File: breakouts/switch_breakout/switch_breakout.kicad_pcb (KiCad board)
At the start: 4 copper layers, 35.5 x 27.8 mm, 10 parts, among them P1 CONN_01X03, U101 CONN_SMA_2GND, U102 CONN_SMA_2GND, U103 CONN_SMA_2GND, U3 PE42521

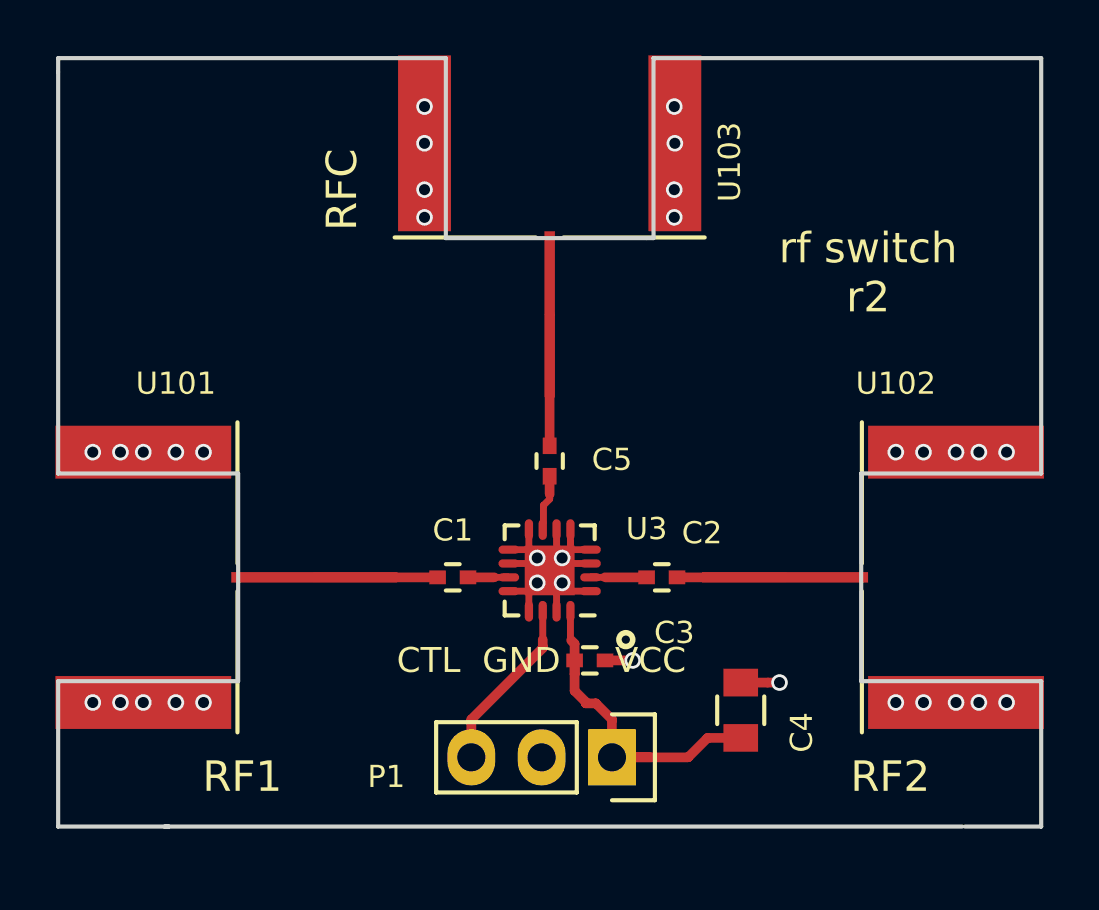
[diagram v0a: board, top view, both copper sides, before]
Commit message: switched switch board to be coplanar waveguide fed
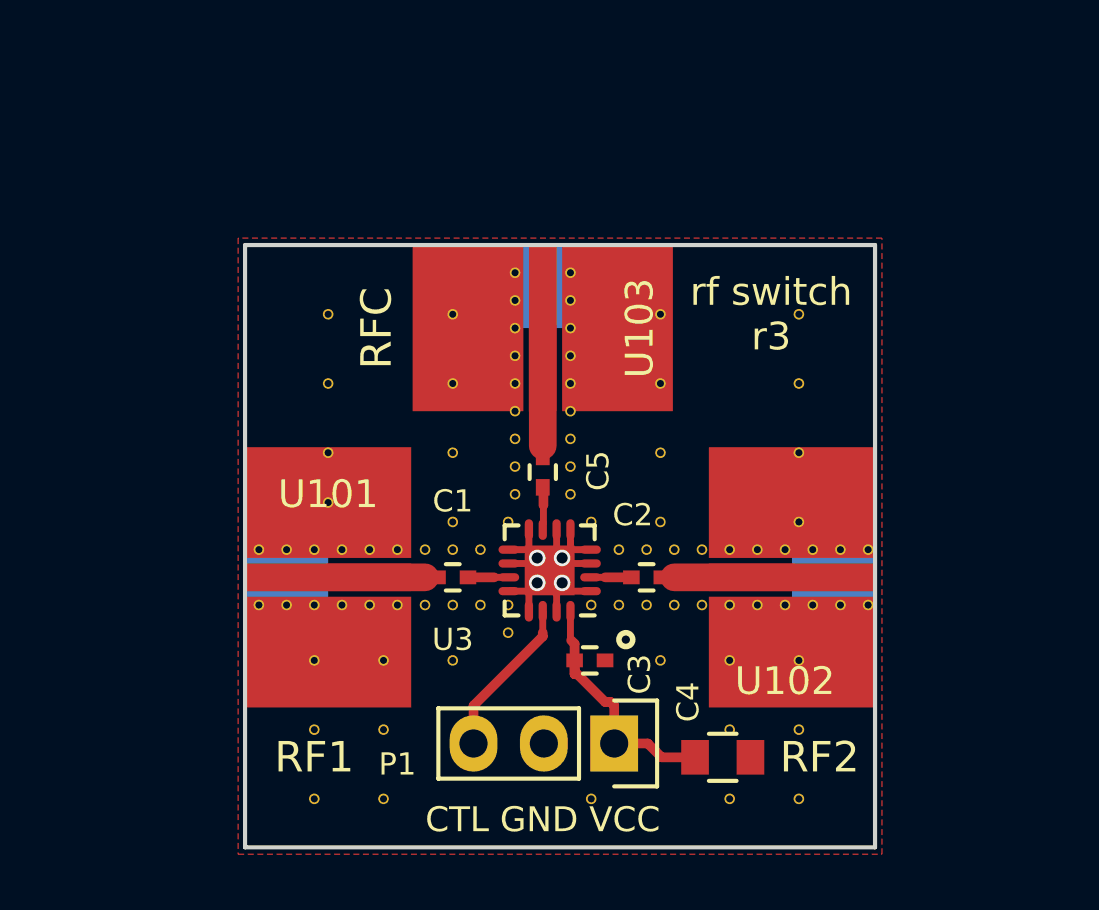
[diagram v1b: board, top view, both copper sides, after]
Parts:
- added REF**: VIA_OSH4LAYER_MIN, vna_footprints:VIA_OSH4LAYER_MIN, F.Cu at (145.0, 110.0)
- added REF**: VIA_OSH4LAYER_MIN, vna_footprints:VIA_OSH4LAYER_MIN, F.Cu at (152.5, 105.0)
- added REF**: VIA_OSH4LAYER_MIN, vna_footprints:VIA_OSH4LAYER_MIN, F.Cu at (145.0, 105.0)
- added REF**: VIA_OSH4LAYER_MIN, vna_footprints:VIA_OSH4LAYER_MIN, F.Cu at (145.0, 102.5)
- added REF**: VIA_OSH4LAYER_MIN, vna_footprints:VIA_OSH4LAYER_MIN, F.Cu at (145.0, 100.0)
- added REF**: VIA_OSH4LAYER_MIN, vna_footprints:VIA_OSH4LAYER_MIN, F.Cu at (145.0, 97.5)
- added REF**: VIA_OSH4LAYER_MIN, vna_footprints:VIA_OSH4LAYER_MIN, F.Cu at (140.5, 97.5)
- added REF**: VIA_OSH4LAYER_MIN, vna_footprints:VIA_OSH4LAYER_MIN, F.Cu at (140.5, 100.0)
- added REF**: VIA_OSH4LAYER_MIN, vna_footprints:VIA_OSH4LAYER_MIN, F.Cu at (140.5, 102.5)
- added REF**: VIA_OSH4LAYER_MIN, vna_footprints:VIA_OSH4LAYER_MIN, F.Cu at (140.5, 104.3)
- added REF**: VIA_OSH4LAYER_MIN, vna_footprints:VIA_OSH4LAYER_MIN, F.Cu at (140.0, 115.0)
- added REF**: VIA_OSH4LAYER_MIN, vna_footprints:VIA_OSH4LAYER_MIN, F.Cu at (150.0, 115.0)
- added REF**: VIA_OSH4LAYER_MIN, vna_footprints:VIA_OSH4LAYER_MIN, F.Cu at (142.5, 115.0)
- added REF**: VIA_OSH4LAYER_MIN, vna_footprints:VIA_OSH4LAYER_MIN, F.Cu at (142.5, 112.5)
- added REF**: VIA_OSH4LAYER_MIN, vna_footprints:VIA_OSH4LAYER_MIN, F.Cu at (140.0, 112.5)
- added REF**: VIA_OSH4LAYER_MIN, vna_footprints:VIA_OSH4LAYER_MIN, F.Cu at (140.0, 110.0)
- added REF**: VIA_OSH4LAYER_MIN, vna_footprints:VIA_OSH4LAYER_MIN, F.Cu at (142.5, 110.0)
- added REF**: VIA_OSH4LAYER_MIN, vna_footprints:VIA_OSH4LAYER_MIN, F.Cu at (157.5, 110.0)
- added REF**: VIA_OSH4LAYER_MIN, vna_footprints:VIA_OSH4LAYER_MIN, F.Cu at (157.5, 112.5)
- added REF**: VIA_OSH4LAYER_MIN, vna_footprints:VIA_OSH4LAYER_MIN, F.Cu at (157.5, 115.0)
- added REF**: VIA_OSH4LAYER_MIN, vna_footprints:VIA_OSH4LAYER_MIN, F.Cu at (155.0, 115.0)
- added REF**: VIA_OSH4LAYER_MIN, vna_footprints:VIA_OSH4LAYER_MIN, F.Cu at (155.0, 112.5)
- added REF**: VIA_OSH4LAYER_MIN, vna_footprints:VIA_OSH4LAYER_MIN, F.Cu at (152.5, 97.5)
- added REF**: VIA_OSH4LAYER_MIN, vna_footprints:VIA_OSH4LAYER_MIN, F.Cu at (155.0, 110.0)
- added REF**: VIA_OSH4LAYER_MIN, vna_footprints:VIA_OSH4LAYER_MIN, F.Cu at (152.5, 110.0)
- added REF**: VIA_OSH4LAYER_MIN, vna_footprints:VIA_OSH4LAYER_MIN, F.Cu at (150.0, 105.0)
- added REF**: VIA_OSH4LAYER_MIN, vna_footprints:VIA_OSH4LAYER_MIN, F.Cu at (149.2, 96.0)
- added REF**: VIA_OSH4LAYER_MIN, vna_footprints:VIA_OSH4LAYER_MIN, F.Cu at (149.2, 97.0)
- added REF**: VIA_OSH4LAYER_MIN, vna_footprints:VIA_OSH4LAYER_MIN, F.Cu at (149.2, 98.0)
- added REF**: VIA_OSH4LAYER_MIN, vna_footprints:VIA_OSH4LAYER_MIN, F.Cu at (149.2, 99.0)
- added REF**: VIA_OSH4LAYER_MIN, vna_footprints:VIA_OSH4LAYER_MIN, F.Cu at (149.2, 100.0)
- added REF**: VIA_OSH4LAYER_MIN, vna_footprints:VIA_OSH4LAYER_MIN, F.Cu at (149.2, 101.0)
- added REF**: VIA_OSH4LAYER_MIN, vna_footprints:VIA_OSH4LAYER_MIN, F.Cu at (149.2, 104.0)
- added REF**: VIA_OSH4LAYER_MIN, vna_footprints:VIA_OSH4LAYER_MIN, F.Cu at (157.5, 97.5)
- added REF**: VIA_OSH4LAYER_MIN, vna_footprints:VIA_OSH4LAYER_MIN, F.Cu at (149.2, 103.0)
- added REF**: VIA_OSH4LAYER_MIN, vna_footprints:VIA_OSH4LAYER_MIN, F.Cu at (149.2, 102.0)
- added REF**: VIA_OSH4LAYER_MIN, vna_footprints:VIA_OSH4LAYER_MIN, F.Cu at (138.0, 108.0)
- added REF**: VIA_OSH4LAYER_MIN, vna_footprints:VIA_OSH4LAYER_MIN, F.Cu at (138.0, 106.0)
- added REF**: VIA_OSH4LAYER_MIN, vna_footprints:VIA_OSH4LAYER_MIN, F.Cu at (139.0, 106.0)
- added REF**: VIA_OSH4LAYER_MIN, vna_footprints:VIA_OSH4LAYER_MIN, F.Cu at (140.0, 106.0)
- added REF**: VIA_OSH4LAYER_MIN, vna_footprints:VIA_OSH4LAYER_MIN, F.Cu at (141.0, 106.0)
- added REF**: VIA_OSH4LAYER_MIN, vna_footprints:VIA_OSH4LAYER_MIN, F.Cu at (142.0, 106.0)
- added REF**: VIA_OSH4LAYER_MIN, vna_footprints:VIA_OSH4LAYER_MIN, F.Cu at (143.0, 106.0)
- added REF**: VIA_OSH4LAYER_MIN, vna_footprints:VIA_OSH4LAYER_MIN, F.Cu at (144.0, 106.0)
- added REF**: VIA_OSH4LAYER_MIN, vna_footprints:VIA_OSH4LAYER_MIN, F.Cu at (157.5, 100.0)
- added REF**: VIA_OSH4LAYER_MIN, vna_footprints:VIA_OSH4LAYER_MIN, F.Cu at (145.0, 106.0)
- added REF**: VIA_OSH4LAYER_MIN, vna_footprints:VIA_OSH4LAYER_MIN, F.Cu at (151.0, 106.0)
- added REF**: VIA_OSH4LAYER_MIN, vna_footprints:VIA_OSH4LAYER_MIN, F.Cu at (152.0, 106.0)
- added REF**: VIA_OSH4LAYER_MIN, vna_footprints:VIA_OSH4LAYER_MIN, F.Cu at (153.0, 106.0)
- added REF**: VIA_OSH4LAYER_MIN, vna_footprints:VIA_OSH4LAYER_MIN, F.Cu at (154.0, 106.0)
- added REF**: VIA_OSH4LAYER_MIN, vna_footprints:VIA_OSH4LAYER_MIN, F.Cu at (155.0, 106.0)
- added REF**: VIA_OSH4LAYER_MIN, vna_footprints:VIA_OSH4LAYER_MIN, F.Cu at (156.0, 106.0)
- added REF**: VIA_OSH4LAYER_MIN, vna_footprints:VIA_OSH4LAYER_MIN, F.Cu at (157.0, 106.0)
- added REF**: VIA_OSH4LAYER_MIN, vna_footprints:VIA_OSH4LAYER_MIN, F.Cu at (158.0, 106.0)
- added REF**: VIA_OSH4LAYER_MIN, vna_footprints:VIA_OSH4LAYER_MIN, F.Cu at (159.0, 106.0)
- added REF**: VIA_OSH4LAYER_MIN, vna_footprints:VIA_OSH4LAYER_MIN, F.Cu at (152.5, 100.0)
- added REF**: VIA_OSH4LAYER_MIN, vna_footprints:VIA_OSH4LAYER_MIN, F.Cu at (160.0, 106.0)
- added REF**: VIA_OSH4LAYER_MIN, vna_footprints:VIA_OSH4LAYER_MIN, F.Cu at (160.0, 108.0)
- added REF**: VIA_OSH4LAYER_MIN, vna_footprints:VIA_OSH4LAYER_MIN, F.Cu at (159.0, 108.0)
- added REF**: VIA_OSH4LAYER_MIN, vna_footprints:VIA_OSH4LAYER_MIN, F.Cu at (158.0, 108.0)
- added REF**: VIA_OSH4LAYER_MIN, vna_footprints:VIA_OSH4LAYER_MIN, F.Cu at (157.0, 108.0)
- added REF**: VIA_OSH4LAYER_MIN, vna_footprints:VIA_OSH4LAYER_MIN, F.Cu at (156.0, 108.0)
- added REF**: VIA_OSH4LAYER_MIN, vna_footprints:VIA_OSH4LAYER_MIN, F.Cu at (155.0, 108.0)
- added REF**: VIA_OSH4LAYER_MIN, vna_footprints:VIA_OSH4LAYER_MIN, F.Cu at (154.0, 108.0)
- added REF**: VIA_OSH4LAYER_MIN, vna_footprints:VIA_OSH4LAYER_MIN, F.Cu at (153.0, 108.0)
- added REF**: VIA_OSH4LAYER_MIN, vna_footprints:VIA_OSH4LAYER_MIN, F.Cu at (152.0, 108.0)
- added REF**: VIA_OSH4LAYER_MIN, vna_footprints:VIA_OSH4LAYER_MIN, F.Cu at (152.5, 102.5)
- added REF**: VIA_OSH4LAYER_MIN, vna_footprints:VIA_OSH4LAYER_MIN, F.Cu at (151.0, 108.0)
- added REF**: VIA_OSH4LAYER_MIN, vna_footprints:VIA_OSH4LAYER_MIN, F.Cu at (150.0, 108.0)
- added REF**: VIA_OSH4LAYER_MIN, vna_footprints:VIA_OSH4LAYER_MIN, F.Cu at (147.2, 96.0)
- added REF**: VIA_OSH4LAYER_MIN, vna_footprints:VIA_OSH4LAYER_MIN, F.Cu at (147.2, 97.0)
- added REF**: VIA_OSH4LAYER_MIN, vna_footprints:VIA_OSH4LAYER_MIN, F.Cu at (147.2, 98.0)
- added REF**: VIA_OSH4LAYER_MIN, vna_footprints:VIA_OSH4LAYER_MIN, F.Cu at (147.2, 99.0)
- added REF**: VIA_OSH4LAYER_MIN, vna_footprints:VIA_OSH4LAYER_MIN, F.Cu at (147.2, 100.0)
- added REF**: VIA_OSH4LAYER_MIN, vna_footprints:VIA_OSH4LAYER_MIN, F.Cu at (147.2, 101.0)
- added REF**: VIA_OSH4LAYER_MIN, vna_footprints:VIA_OSH4LAYER_MIN, F.Cu at (147.2, 102.0)
- added REF**: VIA_OSH4LAYER_MIN, vna_footprints:VIA_OSH4LAYER_MIN, F.Cu at (147.2, 103.0)
- added REF**: VIA_OSH4LAYER_MIN, vna_footprints:VIA_OSH4LAYER_MIN, F.Cu at (157.5, 102.5)
- added REF**: VIA_OSH4LAYER_MIN, vna_footprints:VIA_OSH4LAYER_MIN, F.Cu at (147.2, 104.0)
- added REF**: VIA_OSH4LAYER_MIN, vna_footprints:VIA_OSH4LAYER_MIN, F.Cu at (147.0, 105.0)
- added REF**: VIA_OSH4LAYER_MIN, vna_footprints:VIA_OSH4LAYER_MIN, F.Cu at (146.0, 106.0)
- added REF**: VIA_OSH4LAYER_MIN, vna_footprints:VIA_OSH4LAYER_MIN, F.Cu at (147.0, 109.0)
- added REF**: VIA_OSH4LAYER_MIN, vna_footprints:VIA_OSH4LAYER_MIN, F.Cu at (147.0, 108.0)
- added REF**: VIA_OSH4LAYER_MIN, vna_footprints:VIA_OSH4LAYER_MIN, F.Cu at (146.0, 108.0)
- added REF**: VIA_OSH4LAYER_MIN, vna_footprints:VIA_OSH4LAYER_MIN, F.Cu at (145.0, 108.0)
- added REF**: VIA_OSH4LAYER_MIN, vna_footprints:VIA_OSH4LAYER_MIN, F.Cu at (144.0, 108.0)
- added REF**: VIA_OSH4LAYER_MIN, vna_footprints:VIA_OSH4LAYER_MIN, F.Cu at (143.0, 108.0)
- added REF**: VIA_OSH4LAYER_MIN, vna_footprints:VIA_OSH4LAYER_MIN, F.Cu at (142.0, 108.0)
- added REF**: VIA_OSH4LAYER_MIN, vna_footprints:VIA_OSH4LAYER_MIN, F.Cu at (157.5, 105.0)
- added REF**: VIA_OSH4LAYER_MIN, vna_footprints:VIA_OSH4LAYER_MIN, F.Cu at (141.0, 108.0)
- added REF**: VIA_OSH4LAYER_MIN, vna_footprints:VIA_OSH4LAYER_MIN, F.Cu at (140.0, 108.0)
- added REF**: VIA_OSH4LAYER_MIN, vna_footprints:VIA_OSH4LAYER_MIN, F.Cu at (139.0, 108.0)
- U101, U102, U103: footprint vna_footprints:142-0721-882_sma_cutout -> vna_footprints:SMA_CPW_1MM_.2MM
- moved U103 6.68 mm to (148.2, 98.0), turned to 0 degrees
- moved U101 6.68 mm to (140.5, 107.0), turned to 90 degrees
- moved U102 5.93 mm to (157.2, 107.0), turned to 270 degrees
- moved C4 1.82 mm to (154.8, 113.5), turned to 0 degrees
- moved C2 0.55 mm to (152.0, 107.0)
- moved P1 0.51 mm to (150.8, 113.0)
- moved C5 0.47 mm to (148.2, 103.2)
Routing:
- net Net-(C3-Pad1): track 12.9 -> 9.23 mm
- net GND: track 14.0 -> 13.0 mm, vias 34 -> 4
- net Net-(P1-Pad3): track 6.50 -> 5.81 mm
- net Net-(C2-Pad1): track 4.10 -> 4.70 mm
- net Net-(C2-Pad2): track 2.03 -> 1.47 mm
- net Net-(C1-Pad1): track 4.45 -> 3.95 mm
- added copper zone on F.Cu, net GND
- added copper zone on In2.Cu, net GND
- removed copper zone on In1.Cu, net GND
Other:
- board size 35.5 x 27.8 mm -> 22.8 x 21.8 mm
- rule pad_to_mask_clearance: 0.2 -> 0
- board text added: "2016.11"
- board text added: "rf switch r3"
- board text removed: "2016.04"
- board text removed: "rf switch r2"
